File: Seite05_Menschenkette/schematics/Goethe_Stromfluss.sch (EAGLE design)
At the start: 11 parts, among them M1 ARDUINO_R3_SMALL

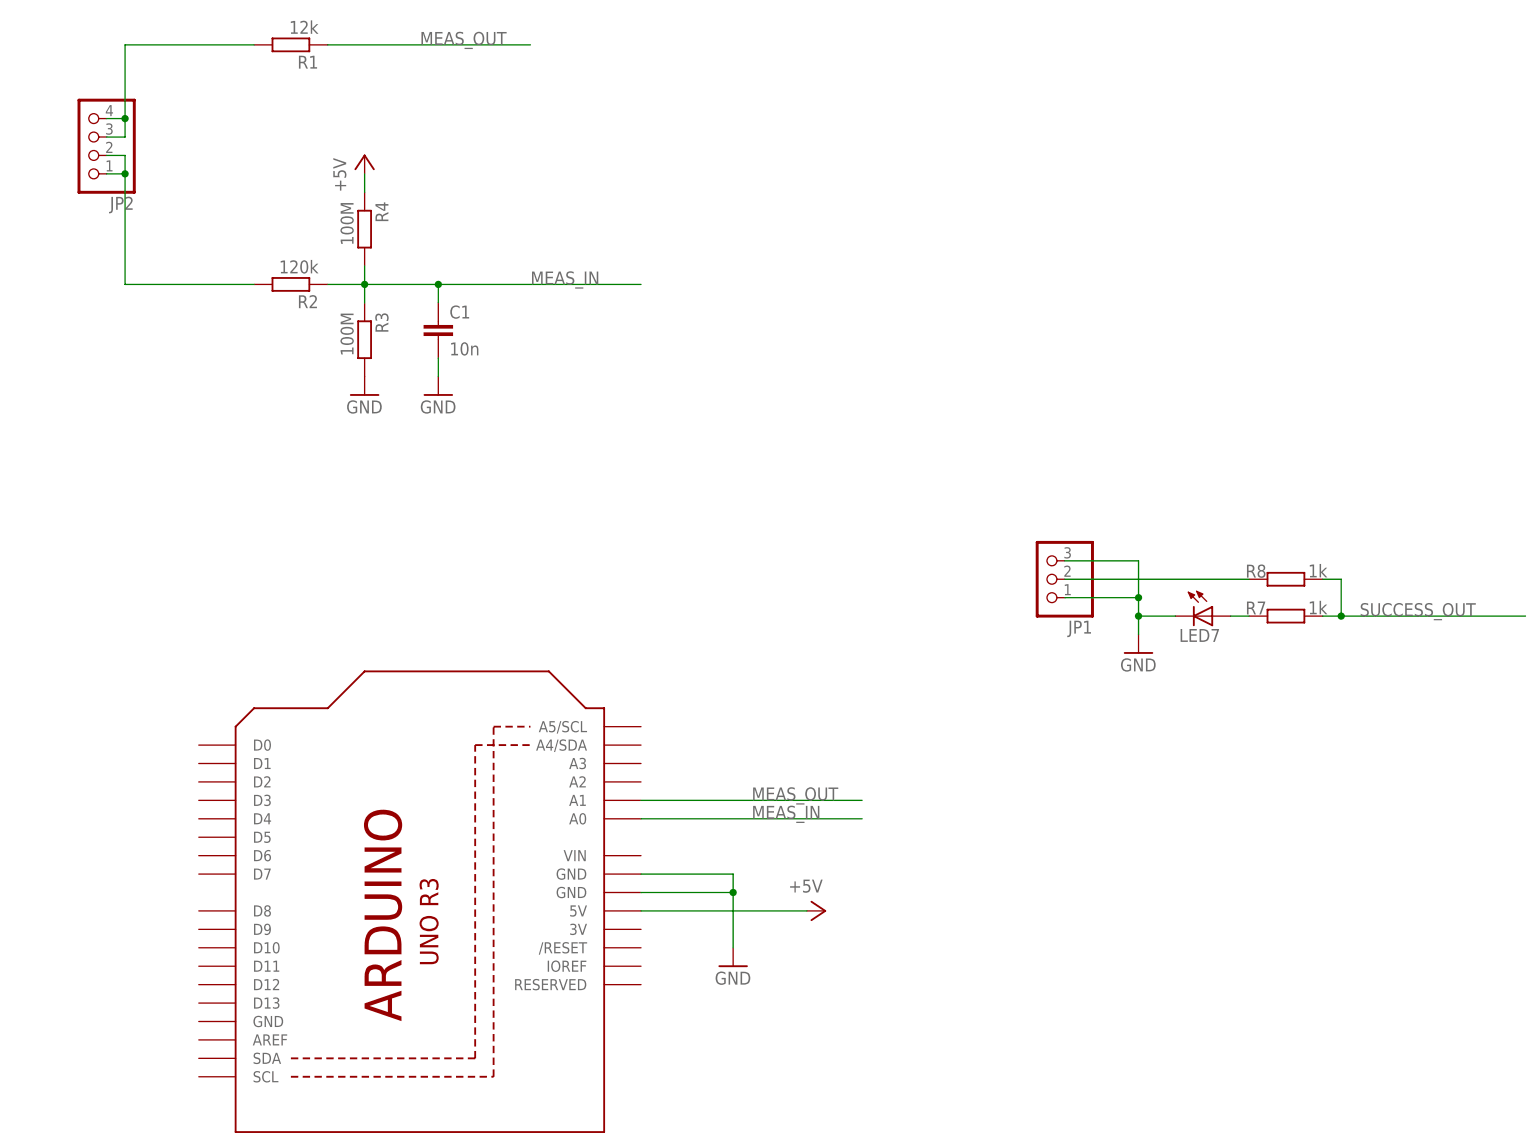
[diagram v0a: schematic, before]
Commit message: RFID detector firmware for new shield v2; Detector firmware for last page with learnable UID
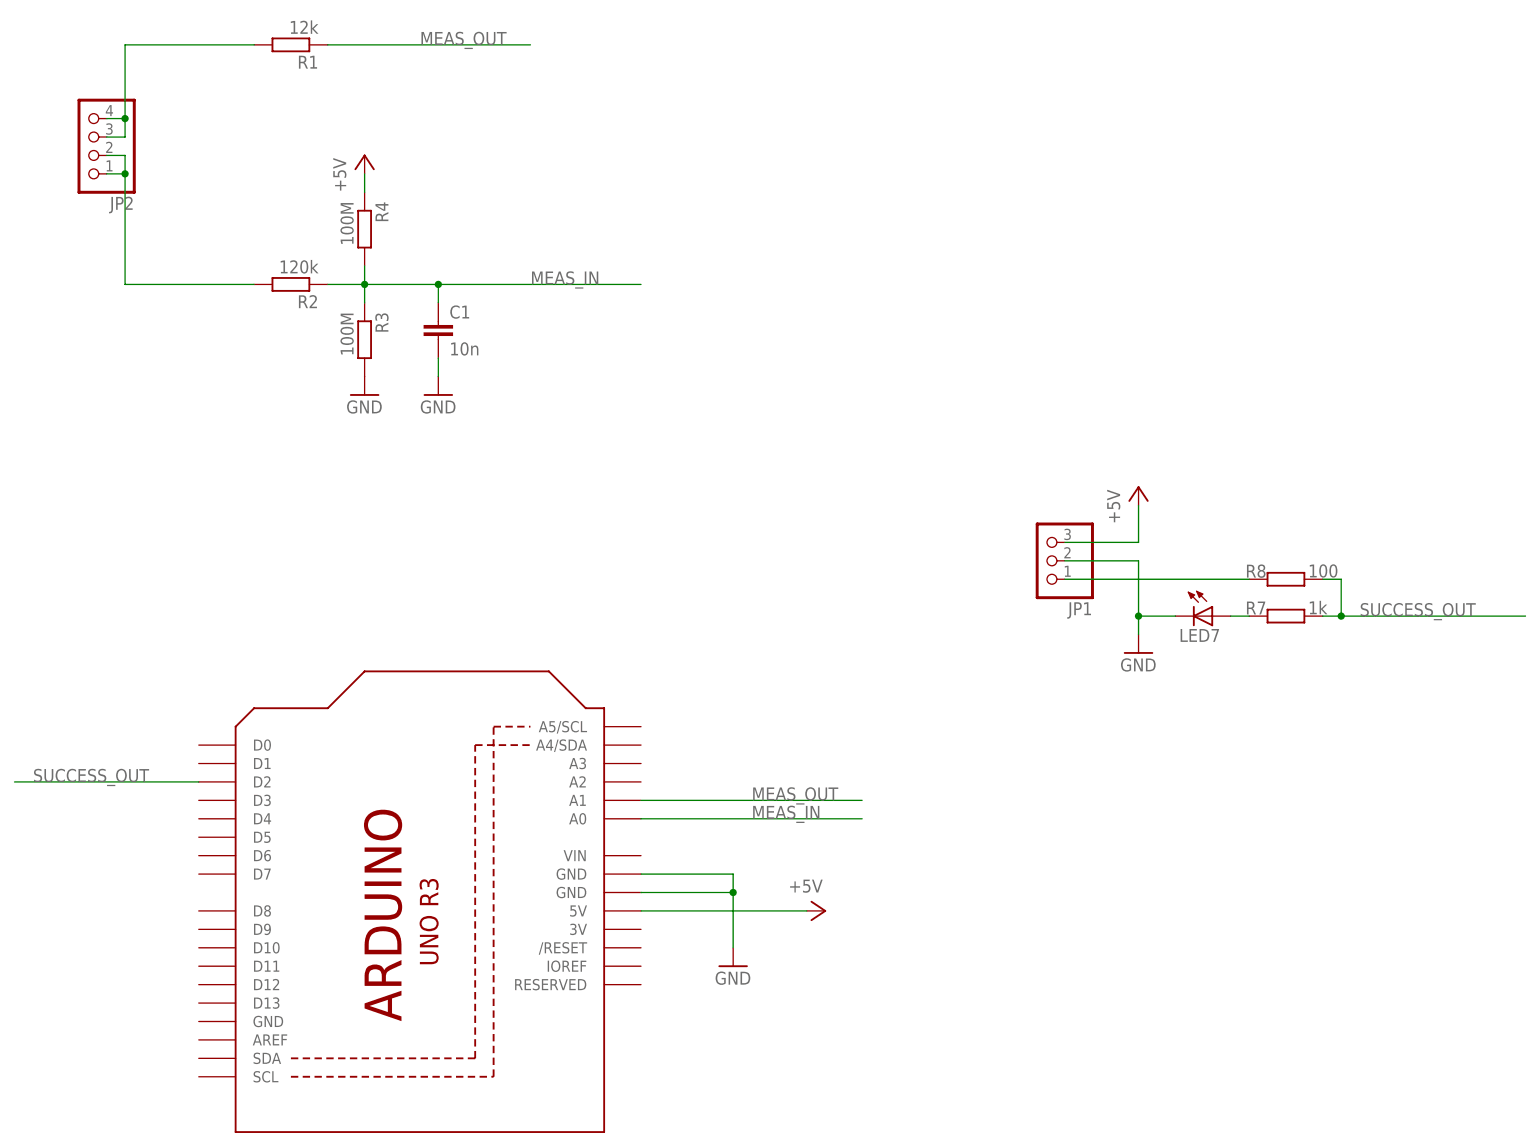
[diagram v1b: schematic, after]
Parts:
- R7: device rcl:R-EU_R0805 -> rcl:R-EU_0204/7
- R8: value 1k -> 100; device rcl:R-EU_R0805 -> rcl:R-EU_0207/12
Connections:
- removed net SUCCESS_OUT_: JP1.2, R8.2
- new net N$2: JP1.1, R8.2
- net +5V: now also JP1.3
- net GND: now also JP1.2; no longer JP1.1, JP1.3
- net SUCCESS_OUT: now also M1.D2
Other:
- moved on the sheet: JP1
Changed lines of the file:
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@@
 <part name="P+5" library="supply1" deviceset="+5V" device=""/>
 <part name="GND16" library="supply1" deviceset="GND" device=""/>
-<part name="R7" library="rcl" deviceset="R-EU_" device="R0805" value="1k"/>
-<part name="R8" library="rcl" deviceset="R-EU_" device="R0805" value="1k"/>
+<part name="R7" library="rcl" deviceset="R-EU_" device="0204/7" value="1k"/>
+<part name="R8" library="rcl" deviceset="R-EU_" device="0207/12" value="100"/>
 <part name="LED7" library="led" deviceset="LED" device="3MM"/>
 <part name="GND18" library="supply1" deviceset="GND" device=""/>
@@
 <part name="GND2" library="supply1" deviceset="GND" device=""/>
 <part name="P+1" library="supply1" deviceset="+5V" device=""/>
+<part name="P+2" library="supply1" deviceset="+5V" device=""/>
 </parts>
 <sheets>
@@
 <instance part="FRAME2" gate="G$1" x="0" y="185.42"/>
 <instance part="FRAME2" gate="G$2" x="162.56" y="185.42"/>
-<instance part="JP1" gate="A" x="167.64" y="276.86" rot="R180"/>
+<instance part="JP1" gate="A" x="167.64" y="279.4" rot="R180"/>
 <instance part="JP2" gate="A" x="35.56" y="337.82" rot="R180"/>
 <instance part="R1" gate="G$1" x="63.5" y="350.52" rot="R180"/>
@@
 <instance part="GND2" gate="1" x="83.82" y="302.26"/>
 <instance part="P+1" gate="1" x="73.66" y="335.28"/>
+<instance part="P+2" gate="1" x="180.34" y="289.56"/>
 </instances>
 <busses>
@@
 <wire x1="180.34" y1="269.24" x2="180.34" y2="271.78" width="0.1524" layer="91"/>
 <wire x1="180.34" y1="271.78" x2="185.42" y2="271.78" width="0.1524" layer="91"/>
-<pinref part="JP1" gate="A" pin="1"/>
-<wire x1="170.18" y1="274.32" x2="180.34" y2="274.32" width="0.1524" layer="91"/>
-<wire x1="180.34" y1="274.32" x2="180.34" y2="271.78" width="0.1524" layer="91"/>
 <junction x="180.34" y="271.78"/>
-<wire x1="180.34" y1="274.32" x2="180.34" y2="279.4" width="0.1524" layer="91"/>
-<junction x="180.34" y="274.32"/>
-<pinref part="JP1" gate="A" pin="3"/>
-<wire x1="180.34" y1="279.4" x2="170.18" y2="279.4" width="0.1524" layer="91"/>
+<wire x1="180.34" y1="271.78" x2="180.34" y2="279.4" width="0.1524" layer="91"/>
+<pinref part="JP1" gate="A" pin="2"/>
+<wire x1="170.18" y1="279.4" x2="180.34" y2="279.4" width="0.1524" layer="91"/>
 </segment>
 <segment>
@@
 <wire x1="73.66" y1="332.74" x2="73.66" y2="330.2" width="0.1524" layer="91"/>
 </segment>
+<segment>
+<pinref part="JP1" gate="A" pin="3"/>
+<wire x1="170.18" y1="281.94" x2="180.34" y2="281.94" width="0.1524" layer="91"/>
+<wire x1="180.34" y1="281.94" x2="180.34" y2="287.02" width="0.1524" layer="91"/>
+<pinref part="P+2" gate="1" pin="+5V"/>
+</segment>
 </net>
 <net name="SUCCESS_OUT" class="0">
@@
 <label x="210.82" y="271.78" size="1.778" layer="95"/>
 </segment>
+<segment>
+<wire x1="25.4" y1="248.92" x2="50.8" y2="248.92" width="0.1524" layer="91"/>
+<label x="27.94" y="248.92" size="1.778" layer="95"/>
+<pinref part="M1" gate="G$1" pin="D2"/>
+</segment>
 </net>
 <net name="N$8" class="0">
@@
 <pinref part="R7" gate="G$1" pin="2"/>
 <wire x1="193.04" y1="271.78" x2="195.58" y2="271.78" width="0.1524" layer="91"/>
-</segment>
-</net>
-<net name="SUCCESS_OUT_" class="0">
-<segment>
-<pinref part="R8" gate="G$1" pin="2"/>
-<wire x1="195.58" y1="276.86" x2="170.18" y2="276.86" width="0.1524" layer="91"/>
-<pinref part="JP1" gate="A" pin="2"/>
 </segment>
 </net>
@@
 </segment>
 </net>
+<net name="N$2" class="0">
+<segment>
+<pinref part="JP1" gate="A" pin="1"/>
+<pinref part="R8" gate="G$1" pin="2"/>
+<wire x1="170.18" y1="276.86" x2="195.58" y2="276.86" width="0.1524" layer="91"/>
+</segment>
+</net>
